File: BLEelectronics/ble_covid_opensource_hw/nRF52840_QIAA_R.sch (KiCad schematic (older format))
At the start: 37 parts, among them J3 Conn_02x05_Odd_Even, U6 nRF52840, X1 32MHz, X2 32.768KHZ

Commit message: hw mvp 1b schematic full draft ready for review
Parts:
- removed AE1: Antenna, symbol Device:Antenna
- C10: renamed from C7; footprint Capacitor_SMD:C_0603_1608Metric -> Capacitor_SMD:C_0201_0603Metric
- C11: renamed from C8; value 0 -> N.C.; footprint Capacitor_SMD:C_0603_1608Metric -> Capacitor_SMD:C_0201_0603Metric
- C12: renamed from C9; footprint Capacitor_SMD:C_0603_1608Metric -> Capacitor_SMD:C_0201_0603Metric
- C13: renamed from C10; footprint Capacitor_SMD:C_0603_1608Metric -> Capacitor_SMD:C_0201_0603Metric
- C14: renamed from C11; footprint Capacitor_SMD:C_0603_1608Metric -> Capacitor_SMD:C_0201_0603Metric
- C15: renamed from C13; footprint Capacitor_SMD:C_0603_1608Metric -> Capacitor_SMD:C_0201_0603Metric
- C16: renamed from C14; footprint Capacitor_SMD:C_0603_1608Metric -> Capacitor_SMD:C_0201_0603Metric
- C17: renamed from C15; value 0 -> N.C.; footprint Capacitor_SMD:C_0603_1608Metric -> Capacitor_SMD:C_0402_1005Metric
- C18: renamed from C16; footprint Capacitor_SMD:C_0603_1608Metric -> Capacitor_SMD:C_0402_1005Metric
- C19: renamed from C17; value 0 -> N.C.; footprint Capacitor_SMD:C_0603_1608Metric -> Capacitor_SMD:C_0402_1005Metric
- C21: renamed from C18; footprint Capacitor_SMD:C_0603_1608Metric -> Capacitor_SMD:C_0402_1005Metric
- C25: renamed from C22; footprint Capacitor_SMD:C_0603_1608Metric -> Capacitor_SMD:C_0201_0603Metric
- C26: renamed from C23; footprint Capacitor_SMD:C_0603_1608Metric -> Capacitor_SMD:C_0201_0603Metric
- C27: renamed from C?; footprint Capacitor_SMD:C_0603_1608Metric -> Capacitor_SMD:C_0201_0603Metric
- D4: footprint (none) -> 0my_footprints:LED_APHF1608SEEQBDZGKC; symbol Device:LED_ABRG -> LED_APHF1608SEEQBDZGKC:APHF1608SEEQBDZGKC; DPN (none) -> 754-2144-1-ND; MFR (none) -> Kingbright; MPN (none) -> APHF1608SEEQBDZGKC
- D5: renamed from D3; footprint (none) -> LED_SMD:LED_0603_1608Metric
- L1: value L -> 3.9nH; footprint Inductor_SMD:L_0402_1005Metric -> Inductor_SMD:L_0201_0603Metric
- R10: renamed from R12; footprint (none) -> Resistor_SMD:R_0201_0603Metric
- R11: renamed from R8; footprint Resistor_SMD:R_0603_1608Metric -> Resistor_SMD:R_0201_0603Metric
- R12: renamed from R?; footprint Resistor_SMD:R_0603_1608Metric_Pad1.05x0.95mm_HandSolder -> Resistor_SMD:R_0201_0603Metric
- R7: renamed from R9; footprint (none) -> Resistor_SMD:R_0201_0603Metric
- R8: renamed from R10; footprint (none) -> Resistor_SMD:R_0201_0603Metric
- R9: renamed from R11; footprint (none) -> Resistor_SMD:R_0201_0603Metric
- SW1, SW2: renamed from SW?; symbol Switch:SW_MEC_5G -> Switch:SW_Push
- renumbered C12 to C20, C19 to C22, C20 to C23, C21 to C24, U6 to U5
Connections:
- net labels added: ANTENNA
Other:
- note added: "Check R for LEDs\n"
- note added: "Circuits taken from the Nordic Dongle layout and \nconfiguration 5, ref in table 146 on pg 586 of Prod Spec v1.1\nBattery/Ext. regulator to VDD, USB enabled.\nThis is for chip QIAA aQFN 73, the non BGA version"
- note added: "Details from Dongle User Guide pg 13 The buttons are active low, \nwhich means that the input will be connected to ground when the \nbutton is activated. The SW1 button has no external pull-up resistor, \nbut the reset button (SW2) has a 10 k pull-up resistor. To use SW1, \nP1.06 must be configured as an input with an internal pull-up resistor."
- note added: "LEDs are active low, which means that writing a logical \nzero '0' to the output pin will illuminate the LED.\nLED footprint and component"
- note removed: "Circuit configuration 5, ref in table 146 on pg 586 of Prod Spec v1.1\nBattery/Ext. regulator to VDD, USB enabled.\nThis is for chip QIAA aQFN 73, the non BGA version"
- note removed: "Confirmed no pull-up/down\nresistors for SPI protocol\nAdd 100nF cap between \nGND and VCC"
- note removed: "Details from Dongle User Guide pg 13\nThe buttons are active low, which means that the input will \nbe connected to ground when the button is activated. \nThe SW1 button has no external pull-up resistor, but the \nreset button (SW2) has a 10 k pull-up resistor. To use SW1, \nP1.06 must be configured as an input with an internal pull-up resistor."
- note removed: "LEDs are active low, which means that writing a logical \nzero '0' to the output pin will illuminate the LED.\nLED footprint and component TBD. Resistor footprint?"
- note removed: "On the Dongle SW2 is also connected to P0.19, P0.21, P0.23, and P0.25. \nThis is done to simplify PCB routing. These GPIOs should not be used \nand should be left as input with no pull or be disconnected by firmware.\nDetails from Pg13 Dongle guide"
- note removed: "The schematics include an optional series resistor on the USB supply for improved immunity to\ntransient overvoltage during VBUS connection. Using the series resistor is recommended for new\ndesigns. Value 4R7 (4.5ohms?) from pae 585"
- note removed: "ToDo:\nCheck series R for LEDs\nUpdate footprints R and C footprints (0603, 0402 etc)\nCheck matching circuit for ANT\n"

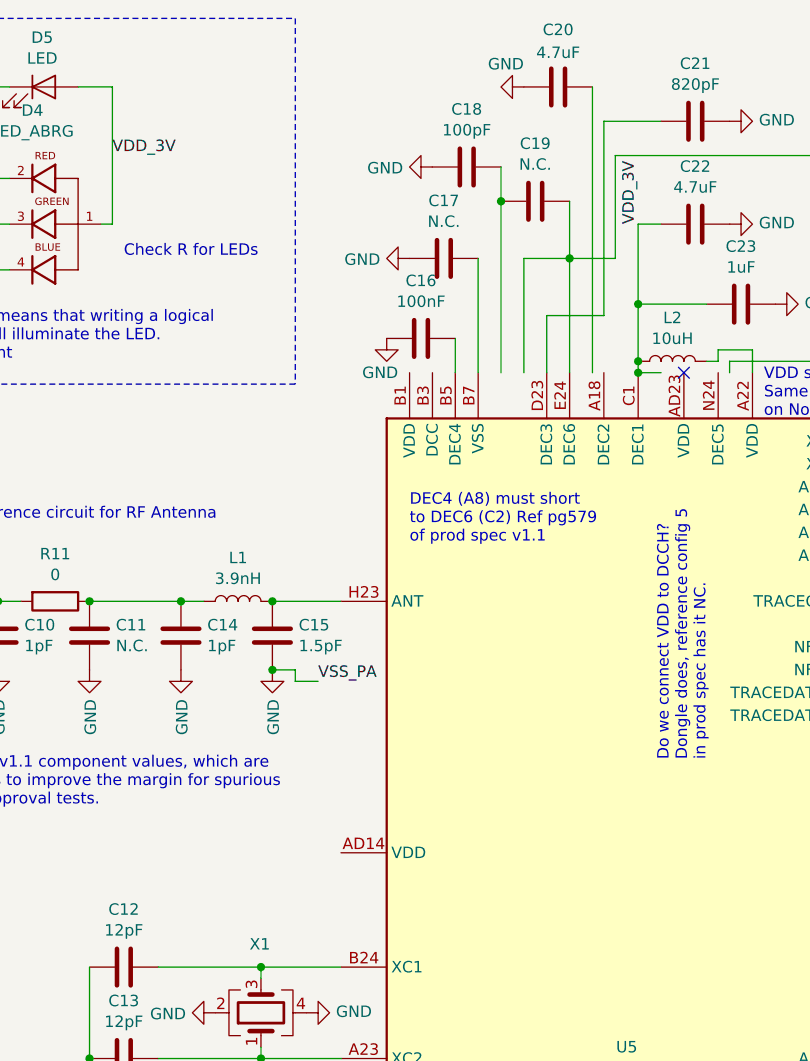
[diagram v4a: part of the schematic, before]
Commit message: Antenna layout implemented
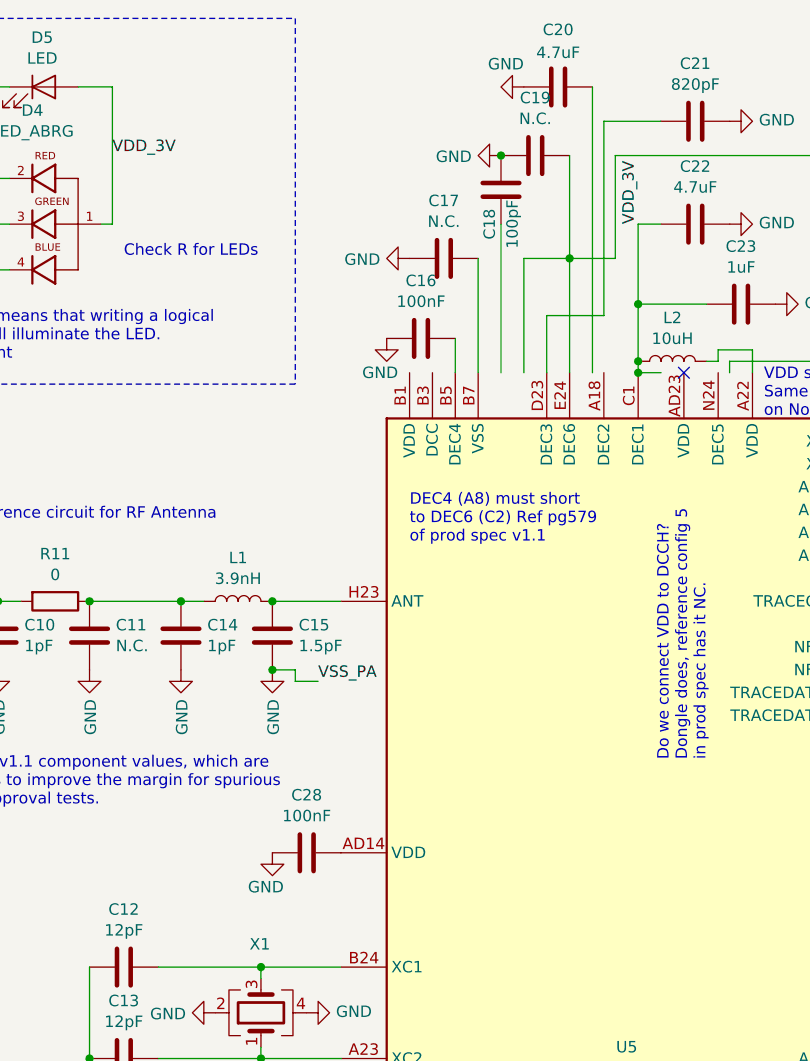
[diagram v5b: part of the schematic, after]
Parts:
- added C28: 100nF, Capacitor_SMD:C_0201_0603Metric, symbol Device:C
- C18, C19: footprint Capacitor_SMD:C_0402_1005Metric -> Capacitor_SMD:C_0201_0603Metric
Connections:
- wire segments 111 -> 110
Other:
- moved on the sheet: C18, C19
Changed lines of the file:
@@
 Comment4 ""
 $EndDescr
-Connection ~ 3850 1350
 Wire Wire Line
 	4300 1000 4300 1850
@@
 	4050 1850 4300 1850
 Connection ~ 4150 1600
-Wire Wire Line
-	4150 1350 4150 1600
 $Comp
 L Device:C C?
 U 1 1 5EC0DD31
-P 4000 1350
+P 4000 1150
 AR Path="/5EC0DD31" Ref="C?"  Part="1"
 AR Path="/5EA608FF/5EC0DD31" Ref="C19"  Part="1"
-F 0 "C19" V 3748 1350 50  0000 C CNN
-F 1 "N.C." V 3839 1350 50  0000 C CNN
-F 2 "Capacitor_SMD:C_0402_1005Metric" H 4038 1200 50  0001 C CNN
-F 3 "~" H 4000 1350 50  0001 C CNN
-	1    4000 1350
+F 0 "C19" V 3748 1150 50  0000 C CNN
+F 1 "N.C." V 3839 1150 50  0000 C CNN
+F 2 "Capacitor_SMD:C_0201_0603Metric" H 4038 1000 50  0001 C CNN
+F 3 "~" H 4000 1150 50  0001 C CNN
+	1    4000 1150
 	0    1    1    0
 $EndComp
 Wire Wire Line
 	3950 1600 4150 1600
-Wire Wire Line
-	3850 1200 3850 1350
 $Comp
 L Device:C C?
 U 1 1 5EC0DD1F
-P 3700 1200
+P 3850 1300
 AR Path="/5EC0DD1F" Ref="C?"  Part="1"
 AR Path="/5EA608FF/5EC0DD1F" Ref="C18"  Part="1"
-F 0 "C18" V 3448 1200 50  0000 C CNN
-F 1 "100pF" V 3539 1200 50  0000 C CNN
-F 2 "Capacitor_SMD:C_0402_1005Metric" H 3738 1050 50  0001 C CNN
-F 3 "~" H 3700 1200 50  0001 C CNN
-	1    3700 1200
-	0    1    1    0
+F 0 "C18" V 3800 1150 50  0000 C CNN
+F 1 "100pF" V 3900 1150 50  0000 C CNN
+F 2 "Capacitor_SMD:C_0201_0603Metric" H 3888 1150 50  0001 C CNN
+F 3 "~" H 3850 1300 50  0001 C CNN
+	1    3850 1300
+	1    0    0    -1
 $EndComp
 $Comp
@@
 	3950 2100 3950 1600
 Wire Wire Line
-	3850 1350 3850 2100
-Wire Wire Line
 	3750 1600 3750 2100
 Wire Wire Line
@@
 	7600 2800 7600 2400
 Connection ~ 7600 2800
-Wire Wire Line
-	5750 2500 6400 2500
 Wire Wire Line
 	5450 1150 5450 1300
@@
 L power:GND #PWR025
 U 1 1 5EC0DD27
-P 3550 1200
+P 3850 1150
 AR Path="/5EA608FF/5EC0DD27" Ref="#PWR025"  Part="1"
 AR Path="/5EC0DD27" Ref="#PWR?"  Part="1"
-F 0 "#PWR025" H 3550 950 50  0001 C CNN
-F 1 "GND" V 3555 1072 50  0000 R CNN
-F 2 "" H 3550 1200 50  0001 C CNN
-F 3 "" H 3550 1200 50  0001 C CNN
-	1    3550 1200
+F 0 "#PWR025" H 3850 900 50  0001 C CNN
+F 1 "GND" V 3855 1022 50  0000 R CNN
+F 2 "" H 3850 1150 50  0001 C CNN
+F 3 "" H 3850 1150 50  0001 C CNN
+	1    3850 1150
 	0    1    1    0
 $EndComp
@@
 	1    1250 850
 	0    1    1    0
-$EndComp
-$Comp
-L MCU_Nordic:nRF52840 U5
-U 1 1 5EC0DD0A
-P 4450 4900
-AR Path="/5EA608FF/5EC0DD0A" Ref="U5"  Part="1"
-AR Path="/5EC0DD0A" Ref="U?"  Part="1"
-F 0 "U5" H 4400 4750 50  0000 C CNN
-F 1 "nRF52840" H 4400 4650 50  0000 C CNN
-F 2 "Package_DFN_QFN:Nordic_AQFN-73-1EP_7x7mm_P0.5mm" H 4450 2000 50  0001 C CNN
-F 3 "http://infocenter.nordicsemi.com/topic/com.nordic.infocenter.nrf52/dita/nrf52/chips/nrf52840.html" H 3800 6800 50  0001 C CNN
-	1    4450 4900
-	1    0    0    -1
 $EndComp
 Wire Notes Line
@@
 Text HLabel 6000 3900 2    50   Input ~ 0
 SCL
-Wire Wire Line
-	6000 3900 5750 3900
 Text HLabel 6000 4100 2    50   Input ~ 0
 CS
@@
 Text HLabel 6000 4700 2    50   Input ~ 0
 SDA
-Wire Wire Line
-	6000 4100 5750 4100
-Wire Wire Line
-	6000 4200 5750 4200
-Wire Wire Line
-	6000 4300 5750 4300
-Wire Wire Line
-	6000 4400 5750 4400
-Wire Wire Line
-	6000 4500 5750 4500
-Wire Wire Line
-	6000 4600 5750 4600
-Wire Wire Line
-	6000 4700 5750 4700
 Text Label 1300 6500 0    50   ~ 0
 VDD_3V
@@
 	9150 3600 9150 5050
 Wire Wire Line
-	6000 6500 5750 6500
-Wire Wire Line
-	6000 6200 5750 6200
-Wire Wire Line
 	6000 7300 5750 7300
-Wire Wire Line
-	6000 7400 5750 7400
-Wire Wire Line
-	6000 3600 5750 3600
-Wire Wire Line
-	6000 3200 5750 3200
-Wire Wire Line
-	6000 3000 5750 3000
 Text Label 6000 6200 2    50   ~ 0
 SW1
@@
 	-1   0    0    -1
 $EndComp
+Wire Wire Line
+	6000 6200 5750 6200
+Wire Wire Line
+	6000 3600 5750 3600
+Wire Wire Line
+	6000 6500 5750 6500
+Wire Wire Line
+	6000 3200 5750 3200
+Wire Wire Line
+	6000 3000 5750 3000
+Wire Wire Line
+	5750 2500 6400 2500
+Wire Wire Line
+	6000 7400 5750 7400
+Wire Wire Line
+	6000 4600 5750 4600
+Wire Wire Line
+	6000 4400 5750 4400
+Wire Wire Line
+	6000 4200 5750 4200
+Wire Wire Line
+	6000 3900 5750 3900
+Wire Wire Line
+	6000 4700 5750 4700
+Wire Wire Line
+	6000 4500 5750 4500
+Wire Wire Line
+	6000 4300 5750 4300
+Wire Wire Line
+	6000 4100 5750 4100
+$Comp
+L MCU_Nordic:nRF52840 U5
+U 1 1 5EC0DD0A
+P 4450 4900
+AR Path="/5EA608FF/5EC0DD0A" Ref="U5"  Part="1"
+AR Path="/5EC0DD0A" Ref="U?"  Part="1"
+F 0 "U5" H 4400 4750 50  0000 C CNN
+F 1 "nRF52840" H 4400 4650 50  0000 C CNN
+F 2 "Package_DFN_QFN:Nordic_AQFN-73-1EP_7x7mm_P0.5mm" H 4450 2000 50  0001 C CNN
+F 3 "http://infocenter.nordicsemi.com/topic/com.nordic.infocenter.nrf52/dita/nrf52/chips/nrf52840.html" H 3800 6800 50  0001 C CNN
+	1    4450 4900
+	1    0    0    -1
+$EndComp
+$Comp
+L Device:C C?
+U 1 1 5EADECF3
+P 3000 4200
+AR Path="/5EADECF3" Ref="C?"  Part="1"
+AR Path="/5EA608FF/5EADECF3" Ref="C28"  Part="1"
+F 0 "C28" V 2748 4200 50  0000 C CNN
+F 1 "100nF" V 2839 4200 50  0000 C CNN
+F 2 "Capacitor_SMD:C_0201_0603Metric" H 3038 4050 50  0001 C CNN
+F 3 "~" H 3000 4200 50  0001 C CNN
+	1    3000 4200
+	0    1    1    0
+$EndComp
+$Comp
+L power:GND #PWR036
+U 1 1 5EADECF9
+P 2850 4200
+AR Path="/5EA608FF/5EADECF9" Ref="#PWR036"  Part="1"
+AR Path="/5EADECF9" Ref="#PWR?"  Part="1"
+F 0 "#PWR036" H 2850 3950 50  0001 C CNN
+F 1 "GND" H 2900 4050 50  0000 R CNN
+F 2 "" H 2850 4200 50  0001 C CNN
+F 3 "" H 2850 4200 50  0001 C CNN
+	1    2850 4200
+	1    0    0    -1
+$EndComp
+Wire Wire Line
+	4150 1150 4150 1600
+Wire Wire Line
+	3850 2100 3850 1450
+Connection ~ 3850 1150
 $EndSCHEMATC

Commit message: hw mvp 1b all components on PCB, todo: traces.
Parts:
- C16: footprint Capacitor_SMD:C_0201_0603Metric -> Capacitor_SMD:C_0402_1005Metric
- C17, C21: footprint Capacitor_SMD:C_0402_1005Metric -> Capacitor_SMD:C_0201_0603Metric
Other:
- moved on the sheet: L3, L4
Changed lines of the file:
@@
 F 0 "C21" V 4952 1000 50  0000 C CNN
 F 1 "820pF" V 4861 1000 50  0000 C CNN
-F 2 "Capacitor_SMD:C_0402_1005Metric" H 4738 850 50  0001 C CNN
+F 2 "Capacitor_SMD:C_0201_0603Metric" H 4738 850 50  0001 C CNN
 F 3 "~" H 4700 1000 50  0001 C CNN
 	1    4700 1000
@@
 F 0 "C17" V 3348 1600 50  0000 C CNN
 F 1 "N.C." V 3439 1600 50  0000 C CNN
-F 2 "Capacitor_SMD:C_0402_1005Metric" H 3638 1450 50  0001 C CNN
+F 2 "Capacitor_SMD:C_0201_0603Metric" H 3638 1450 50  0001 C CNN
 F 3 "~" H 3600 1600 50  0001 C CNN
 	1    3600 1600
@@
 F 0 "C16" V 3248 1950 50  0000 C CNN
 F 1 "100nF" V 3339 1950 50  0000 C CNN
-F 2 "Capacitor_SMD:C_0201_0603Metric" H 3538 1800 50  0001 C CNN
+F 2 "Capacitor_SMD:C_0402_1005Metric" H 3538 1800 50  0001 C CNN
 F 3 "~" H 3500 1950 50  0001 C CNN
 	1    3500 1950
@@
 L Device:L L3
 U 1 1 5EC4EE6E
+P 5450 1850
+F 0 "L3" H 5503 1896 50  0000 L CNN
+F 1 "10uH" H 5503 1805 50  0000 L CNN
+F 2 "Inductor_SMD:L_0603_1608Metric" H 5450 1850 50  0001 C CNN
+F 3 "~" H 5450 1850 50  0001 C CNN
+	1    5450 1850
+	1    0    0    -1
+$EndComp
+$Comp
+L Device:L L4
+U 1 1 5EC4E3E1
 P 5450 1450
-F 0 "L3" H 5503 1496 50  0000 L CNN
-F 1 "10uH" H 5503 1405 50  0000 L CNN
-F 2 "Inductor_SMD:L_0603_1608Metric" H 5450 1450 50  0001 C CNN
+F 0 "L4" H 5503 1496 50  0000 L CNN
+F 1 "15nH" H 5503 1405 50  0000 L CNN
+F 2 "Inductor_SMD:L_0402_1005Metric" H 5450 1450 50  0001 C CNN
 F 3 "~" H 5450 1450 50  0001 C CNN
 	1    5450 1450
 	1    0    0    -1
 $EndComp
-$Comp
-L Device:L L4
-U 1 1 5EC4E3E1
-P 5450 1850
-F 0 "L4" H 5503 1896 50  0000 L CNN
-F 1 "15nH" H 5503 1805 50  0000 L CNN
-F 2 "Inductor_SMD:L_0402_1005Metric" H 5450 1850 50  0001 C CNN
-F 3 "~" H 5450 1850 50  0001 C CNN
-	1    5450 1850
-	1    0    0    -1
-$EndComp
